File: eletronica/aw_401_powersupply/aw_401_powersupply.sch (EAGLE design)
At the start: 64 parts, among them IC1 LM317, IC2 ATTINY2313, IC3 7805, IC4 OPA336P, IC5 ICL7660CPA, IC6 4511N, IC7 74LS138N, IC8 ULN2803, IC9 74AC11139, T1 2N1613

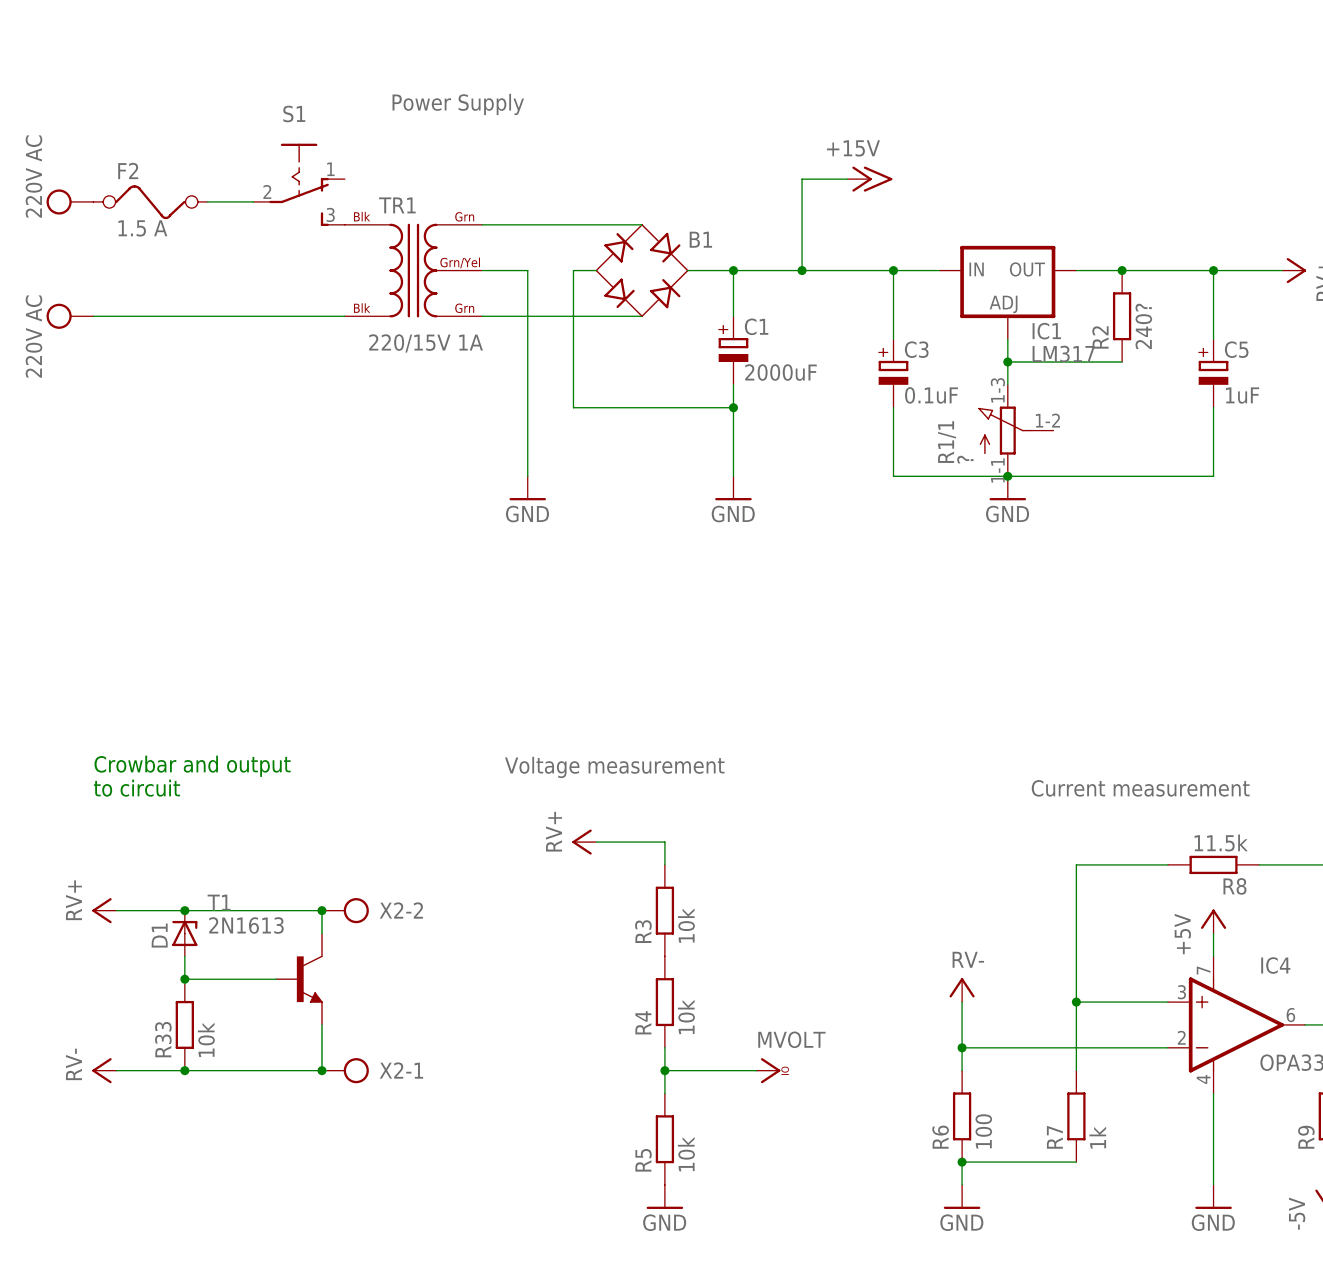
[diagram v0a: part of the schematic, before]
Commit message: 
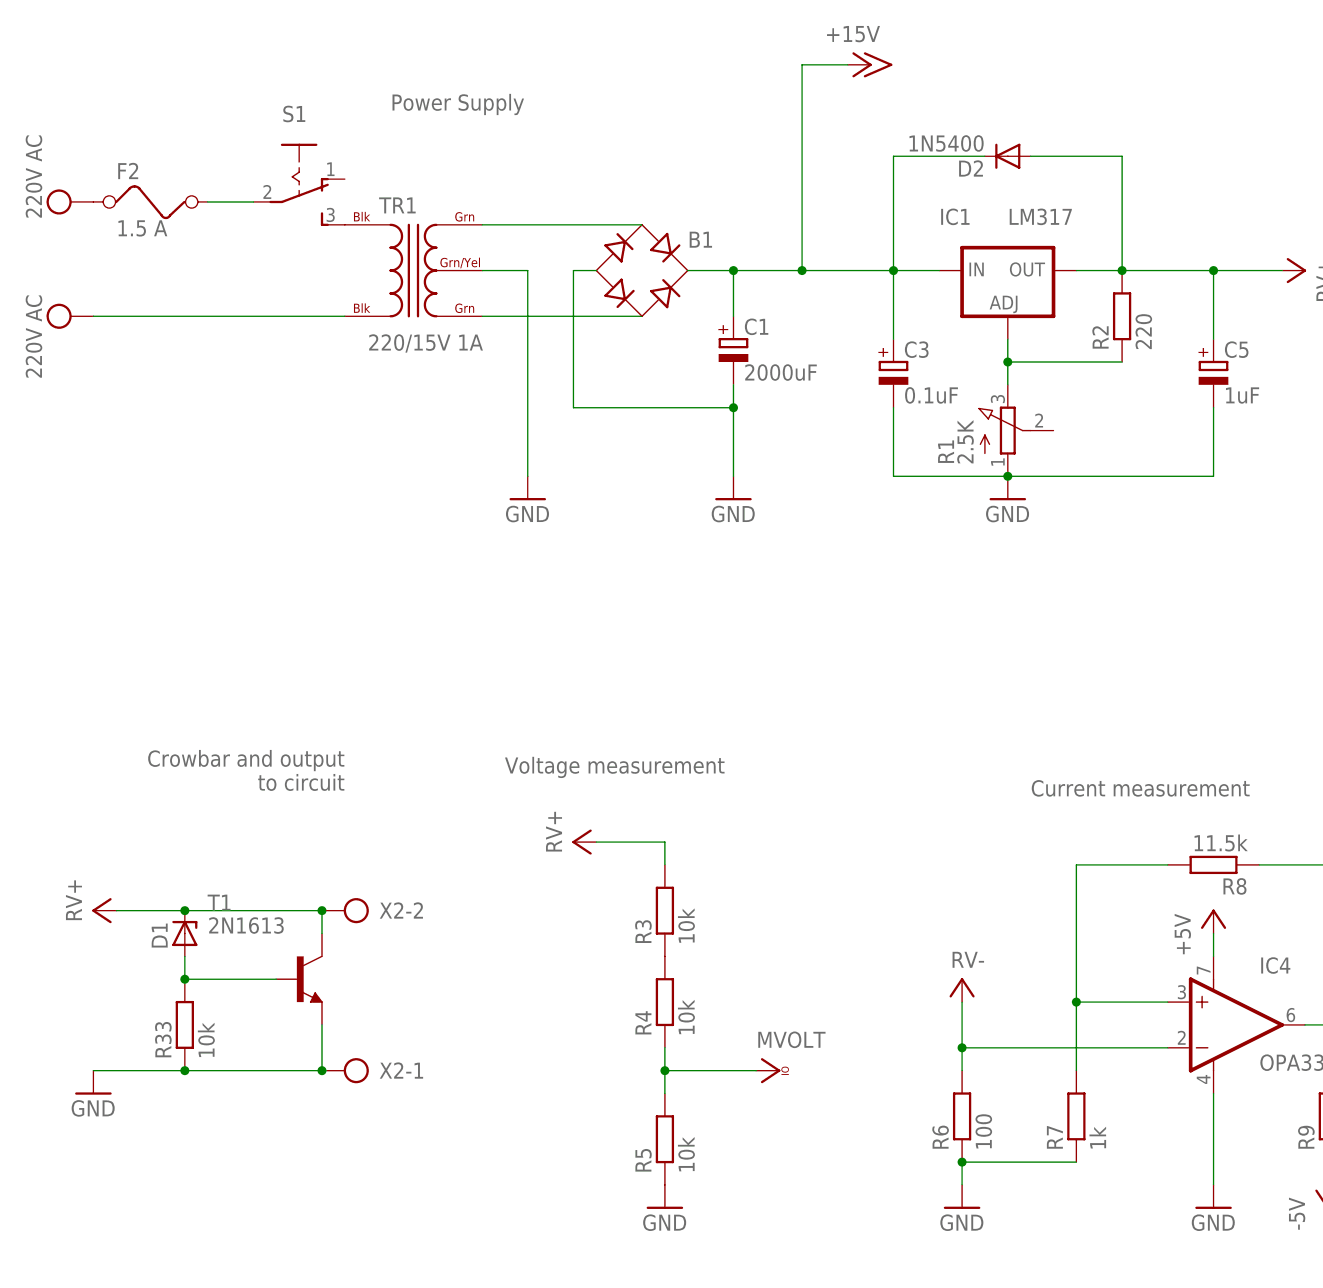
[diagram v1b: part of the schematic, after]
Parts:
- added D2: 1N5400, diode:1N5400
- R1: value ? -> 2.5K; device pot:3RP/1610G -> pot:3RP/1610N
- R2: value 240? -> 220
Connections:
- net +15V: now also D2.C
- net GND: now also R1.A, R33.1, T1.E, X2-1.KL; no longer R1/1.A
- net N$6: now also R1.E; no longer R1/1.E
- net V+: now also D2.A; no longer R33.1, T1.E, X2-1.KL
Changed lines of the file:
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@@
 <part name="GND1" library="supply1" deviceset="GND" device=""/>
 <part name="IC1" library="v-reg" deviceset="LM317TS" device="" value="LM317"/>
-<part name="R1" library="pot" deviceset="3RP/1610G" device="" value="?"/>
 <part name="GND2" library="supply1" deviceset="GND" device=""/>
 <part name="C3" library="resistor" deviceset="CPOL-EU" device="E2.5-6" value="0.1uF"/>
-<part name="R2" library="rcl" deviceset="R-EU_" device="0207/10" value="240?"/>
+<part name="R2" library="rcl" deviceset="R-EU_" device="0207/10" value="220"/>
 <part name="C5" library="resistor" deviceset="CPOL-EU" device="E2.5-6" value="1uF"/>
 <part name="SUPPLY3" library="supply2" deviceset="V+" device="" value="RV+"/>
@@
 <part name="SUPPLY5" library="supply2" deviceset="V+" device="" value="RV+"/>
 <part name="X2" library="con-ptr500" deviceset="AK500/2" device=""/>
-<part name="SUPPLY6" library="supply2" deviceset="V+" device="" value="RV-"/>
 <part name="D1" library="diode" deviceset="ZENER-DIODE" device="C1702-15"/>
 <part name="R33" library="rcl" deviceset="R-EU_" device="0207/10" value="10k"/>
 <part name="T1" library="transistor" deviceset="2N1613" device=""/>
+<part name="R1" library="pot" deviceset="3RP/1610N" device="" value="2.5K"/>
+<part name="D2" library="diode" deviceset="1N5400" device=""/>
+<part name="GND14" library="supply1" deviceset="GND" device=""/>
 </parts>
 <sheets>
@@
 <text x="157.48" y="218.44" size="1.778" layer="95">+15V to +5V converter</text>
 <text x="271.78" y="218.44" size="1.778" layer="95">Voltage/current output</text>
-<text x="15.24" y="142.24" size="1.778" layer="91">Crowbar and output
+<text x="43.18" y="147.32" size="1.778" layer="95" rot="R180">Crowbar and output
 to circuit</text>
 </plain>
@@
 <instance part="C1" gate="G$1" x="86.36" y="193.04"/>
 <instance part="GND1" gate="1" x="86.36" y="175.26"/>
-<instance part="IC1" gate="1" x="116.84" y="200.66"/>
-<instance part="R1" gate="/1" x="116.84" y="182.88"/>
+<instance part="IC1" gate="1" x="116.84" y="200.66" smashed="yes">
+<attribute name="NAME" x="109.22" y="205.74" size="1.778" layer="95"/>
+<attribute name="VALUE" x="116.84" y="205.74" size="1.778" layer="96"/>
+</instance>
 <instance part="GND2" gate="1" x="116.84" y="175.26"/>
 <instance part="C3" gate="G$1" x="104.14" y="190.5"/>
@@
 <instance part="GND9" gate="1" x="226.06" y="149.86"/>
 <instance part="P-2" gate="1" x="236.22" y="170.18" rot="R90"/>
-<instance part="P+4" gate="1" x="101.6" y="210.82" rot="R270"/>
+<instance part="P+4" gate="1" x="101.6" y="223.52" rot="R270"/>
 <instance part="P+5" gate="1" x="172.72" y="200.66" rot="R90"/>
 <instance part="P+2" gate="1" x="236.22" y="200.66" rot="R270"/>
@@
 <instance part="X2" gate="-1" x="45.72" y="111.76" rot="R180"/>
 <instance part="X2" gate="-2" x="45.72" y="129.54" rot="R180"/>
-<instance part="SUPPLY6" gate="1" x="15.24" y="111.76" rot="R90"/>
 <instance part="D1" gate="G$1" x="25.4" y="127" rot="R90"/>
 <instance part="R33" gate="G$1" x="25.4" y="116.84" rot="R90"/>
 <instance part="T1" gate="G$1" x="38.1" y="121.92"/>
+<instance part="R1" gate="G$1" x="116.84" y="182.88"/>
+<instance part="D2" gate="1" x="116.84" y="213.36" rot="R180"/>
+<instance part="GND14" gate="1" x="15.24" y="109.22"/>
 </instances>
 <busses>
@@
 <net name="GND" class="0">
 <segment>
-<pinref part="R1" gate="/1" pin="A"/>
 <pinref part="GND2" gate="1" pin="GND"/>
 <pinref part="C3" gate="G$1" pin="-"/>
@@
 <wire x1="116.84" y1="177.8" x2="139.7" y2="177.8" width="0.1524" layer="91"/>
 <wire x1="139.7" y1="177.8" x2="139.7" y2="185.42" width="0.1524" layer="91"/>
+<pinref part="R1" gate="G$1" pin="A"/>
 </segment>
 <segment>
@@
 <wire x1="63.5" y1="200.66" x2="58.42" y2="200.66" width="0.1524" layer="91"/>
 </segment>
+<segment>
+<pinref part="R33" gate="G$1" pin="1"/>
+<wire x1="15.24" y1="111.76" x2="25.4" y2="111.76" width="0.1524" layer="91"/>
+<pinref part="T1" gate="G$1" pin="E"/>
+<wire x1="25.4" y1="111.76" x2="40.64" y2="111.76" width="0.1524" layer="91"/>
+<wire x1="40.64" y1="111.76" x2="40.64" y2="116.84" width="0.1524" layer="91"/>
+<junction x="25.4" y="111.76"/>
+<pinref part="X2" gate="-1" pin="KL"/>
+<junction x="40.64" y="111.76"/>
+<pinref part="GND14" gate="1" pin="GND"/>
+</segment>
 </net>
 <net name="N$6" class="0">
 <segment>
 <pinref part="IC1" gate="1" pin="ADJ"/>
-<pinref part="R1" gate="/1" pin="E"/>
 <wire x1="116.84" y1="187.96" x2="116.84" y2="190.5" width="0.1524" layer="91"/>
 <pinref part="R2" gate="G$1" pin="1"/>
@@
 <wire x1="129.54" y1="190.5" x2="116.84" y2="190.5" width="0.1524" layer="91"/>
 <junction x="116.84" y="190.5"/>
+<pinref part="R1" gate="G$1" pin="E"/>
 </segment>
 </net>
@@
 <junction x="139.7" y="200.66"/>
 <pinref part="SUPPLY3" gate="1" pin="V+"/>
+<pinref part="D2" gate="1" pin="A"/>
+<wire x1="129.54" y1="200.66" x2="129.54" y2="213.36" width="0.1524" layer="91"/>
+<wire x1="129.54" y1="213.36" x2="119.38" y2="213.36" width="0.1524" layer="91"/>
 </segment>
 <segment>
@@
 <pinref part="X2" gate="-2" pin="KL"/>
 <junction x="40.64" y="129.54"/>
-</segment>
-<segment>
-<pinref part="SUPPLY6" gate="1" pin="V+"/>
-<pinref part="R33" gate="G$1" pin="1"/>
-<wire x1="17.78" y1="111.76" x2="25.4" y2="111.76" width="0.1524" layer="91"/>
-<pinref part="T1" gate="G$1" pin="E"/>
-<wire x1="25.4" y1="111.76" x2="40.64" y2="111.76" width="0.1524" layer="91"/>
-<wire x1="40.64" y1="111.76" x2="40.64" y2="116.84" width="0.1524" layer="91"/>
-<junction x="25.4" y="111.76"/>
-<pinref part="X2" gate="-1" pin="KL"/>
-<junction x="40.64" y="111.76"/>
 </segment>
 </net>
@@
 <junction x="104.14" y="200.66"/>
 <wire x1="93.98" y1="200.66" x2="104.14" y2="200.66" width="0.1524" layer="91"/>
-<wire x1="93.98" y1="200.66" x2="93.98" y2="210.82" width="0.1524" layer="91"/>
-<wire x1="93.98" y1="210.82" x2="99.06" y2="210.82" width="0.1524" layer="91"/>
+<wire x1="93.98" y1="200.66" x2="93.98" y2="223.52" width="0.1524" layer="91"/>
+<wire x1="93.98" y1="223.52" x2="99.06" y2="223.52" width="0.1524" layer="91"/>
 <pinref part="P+4" gate="1" pin="+15V"/>
 <pinref part="B1" gate="1" pin="+"/>
@@
 <junction x="86.36" y="200.66"/>
 <junction x="93.98" y="200.66"/>
-</segment>
-<segment>
+<pinref part="D2" gate="1" pin="C"/>
+<wire x1="114.3" y1="213.36" x2="104.14" y2="213.36" width="0.1524" layer="91"/>
+<wire x1="104.14" y1="213.36" x2="104.14" y2="200.66" width="0.1524" layer="91"/>
+</segment>
+<segment>
